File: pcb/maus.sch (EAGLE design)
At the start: 82 parts, among them IC1 AD712R, Q1 BC817, Q2 BC817, Q3 BSL307SP, T1 BC847, T2 BC847, U1 ESP32-S2-WROOM, U2 CH340C, U3 CP2102, U4 LP3965EMP-3.3, U5 LSM9DS1TR

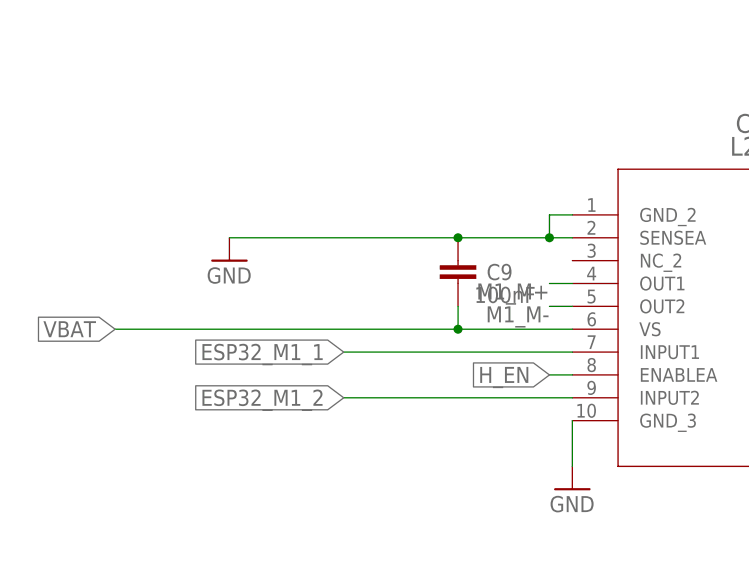
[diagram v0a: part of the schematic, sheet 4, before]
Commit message: Added 3.3V connection
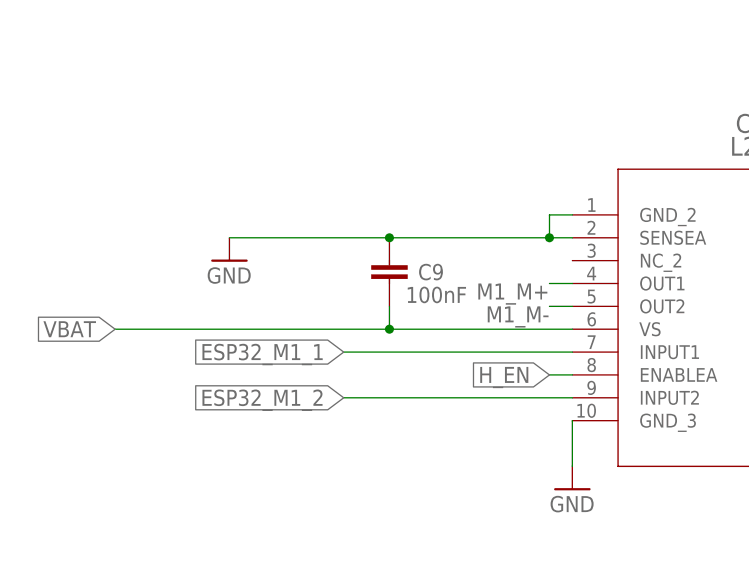
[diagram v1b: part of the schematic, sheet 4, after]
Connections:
- removed net N$2: C3.1, U2.V3
- net +3V3: now also C3.1, U2.V3
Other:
- moved on the sheet: C9
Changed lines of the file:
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@@
 <part name="GND40" library="supply1" library_urn="urn:adsk.eagle:library:371" deviceset="GND" device=""/>
 <part name="JP4" library="pinhead" library_urn="urn:adsk.eagle:library:325" deviceset="PINHD-1X6" device="" package3d_urn="urn:adsk.eagle:package:22472/2"/>
+<part name="+3V10" library="supply1" library_urn="urn:adsk.eagle:library:371" deviceset="+3V3" device=""/>
 </parts>
 <sheets>
@@
 <attribute name="VALUE" x="300.99" y="121.92" size="1.778" layer="96"/>
 </instance>
+<instance part="+3V10" gate="G$1" x="213.36" y="63.5" smashed="yes">
+<attribute name="VALUE" x="210.82" y="58.42" size="1.778" layer="96" rot="R90"/>
+</instance>
 </instances>
 <busses>
@@
 </segment>
 </net>
-<net name="N$2" class="0">
-<segment>
-<pinref part="U2" gate="G$1" pin="V3"/>
-<pinref part="C3" gate="G$1" pin="1"/>
-<wire x1="195.58" y1="55.88" x2="213.36" y2="55.88" width="0.1524" layer="91"/>
-</segment>
-</net>
 <net name="ESP32_TX" class="0">
 <segment>
@@
 <pinref part="+3V1" gate="G$1" pin="+3V3"/>
 <pinref part="JP4" gate="A" pin="5"/>
+</segment>
+<segment>
+<pinref part="U2" gate="G$1" pin="V3"/>
+<pinref part="C3" gate="G$1" pin="1"/>
+<wire x1="195.58" y1="55.88" x2="213.36" y2="55.88" width="0.1524" layer="91"/>
+<pinref part="+3V10" gate="G$1" pin="+3V3"/>
+<wire x1="213.36" y1="55.88" x2="213.36" y2="60.96" width="0.1524" layer="91"/>
+<junction x="213.36" y="55.88"/>
 </segment>
 </net>
@@
 </sheet>
 <sheet>
+<description>H-bridge motor driver</description>
 <plain>
 <text x="40.64" y="109.22" size="1.778" layer="91">Left Motor connector</text>
@@
 <attribute name="VALUE" x="123.444" y="15.621" size="1.778" layer="96"/>
 </instance>
-<instance part="C9" gate="G$1" x="60.96" y="35.56" smashed="yes" rot="R180">
-<attribute name="NAME" x="67.056" y="37.719" size="1.778" layer="95" rot="R180"/>
-<attribute name="VALUE" x="69.596" y="35.179" size="1.778" layer="96" rot="R180"/>
+<instance part="C9" gate="G$1" x="53.34" y="35.56" smashed="yes" rot="R180">
+<attribute name="NAME" x="59.436" y="37.719" size="1.778" layer="95" rot="R180"/>
+<attribute name="VALUE" x="61.976" y="35.179" size="1.778" layer="96" rot="R180"/>
 </instance>
 <instance part="GND31" gate="1" x="121.92" y="10.16" smashed="yes">
@@
 <pinref part="CR1" gate="A" pin="SENSEA"/>
 <wire x1="73.66" y1="40.64" x2="71.12" y2="40.64" width="0.1524" layer="91"/>
-<wire x1="71.12" y1="40.64" x2="60.96" y2="40.64" width="0.1524" layer="91"/>
+<wire x1="71.12" y1="40.64" x2="53.34" y2="40.64" width="0.1524" layer="91"/>
 <pinref part="CR1" gate="A" pin="GND_2"/>
 <wire x1="73.66" y1="43.18" x2="71.12" y2="43.18" width="0.1524" layer="91"/>
@@
 <junction x="71.12" y="40.64"/>
 <pinref part="C9" gate="G$1" pin="2"/>
-<junction x="60.96" y="40.64"/>
+<junction x="53.34" y="40.64"/>
 <pinref part="GND34" gate="1" pin="GND"/>
-<wire x1="60.96" y1="40.64" x2="35.56" y2="40.64" width="0.1524" layer="91"/>
+<wire x1="53.34" y1="40.64" x2="35.56" y2="40.64" width="0.1524" layer="91"/>
 </segment>
 <segment>
@@
 <segment>
 <pinref part="CR1" gate="A" pin="VS"/>
-<wire x1="73.66" y1="30.48" x2="60.96" y2="30.48" width="0.1524" layer="91"/>
-<wire x1="60.96" y1="30.48" x2="60.96" y2="33.02" width="0.1524" layer="91"/>
+<wire x1="73.66" y1="30.48" x2="53.34" y2="30.48" width="0.1524" layer="91"/>
+<wire x1="53.34" y1="30.48" x2="53.34" y2="33.02" width="0.1524" layer="91"/>
 <pinref part="C9" gate="G$1" pin="1"/>
-<junction x="60.96" y="30.48"/>
+<junction x="53.34" y="30.48"/>
 <label x="22.86" y="30.48" size="1.778" layer="95" rot="R180" xref="yes"/>
-<wire x1="60.96" y1="30.48" x2="22.86" y2="30.48" width="0.1524" layer="91"/>
-</segment>
-</net>
+<wire x1="53.34" y1="30.48" x2="22.86" y2="30.48" width="0.1524" layer="91"/>
+</segment>
+</net>

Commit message: Changed capacitor
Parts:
- C8, C9: device rcl:C-EU025-024X044 -> rcl:C-EUC0805
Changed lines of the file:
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@@
 <part name="JP2" library="pinhead" library_urn="urn:adsk.eagle:library:325" deviceset="PINHD-1X3" device="" package3d_urn="urn:adsk.eagle:package:22458/2"/>
 <part name="JP3" library="pinhead" library_urn="urn:adsk.eagle:library:325" deviceset="PINHD-1X3" device="" package3d_urn="urn:adsk.eagle:package:22458/2"/>
-<part name="C8" library="rcl" library_urn="urn:adsk.eagle:library:334" deviceset="C-EU" device="025-024X044" package3d_urn="urn:adsk.eagle:package:23630/1" value="100nF"/>
-<part name="C9" library="rcl" library_urn="urn:adsk.eagle:library:334" deviceset="C-EU" device="025-024X044" package3d_urn="urn:adsk.eagle:package:23630/1" value="100nF"/>
+<part name="C8" library="rcl" library_urn="urn:adsk.eagle:library:334" deviceset="C-EU" device="C0805" package3d_urn="urn:adsk.eagle:package:23617/2" value="100nF"/>
+<part name="C9" library="rcl" library_urn="urn:adsk.eagle:library:334" deviceset="C-EU" device="C0805" package3d_urn="urn:adsk.eagle:package:23617/2" value="100nF"/>
 <part name="IC1" library="analog-devices" library_urn="urn:adsk.eagle:library:102" deviceset="AD712" device="R" package3d_urn="urn:adsk.eagle:package:30987/2"/>
 <part name="P+2" library="supply1" library_urn="urn:adsk.eagle:library:371" deviceset="+5V" device=""/>

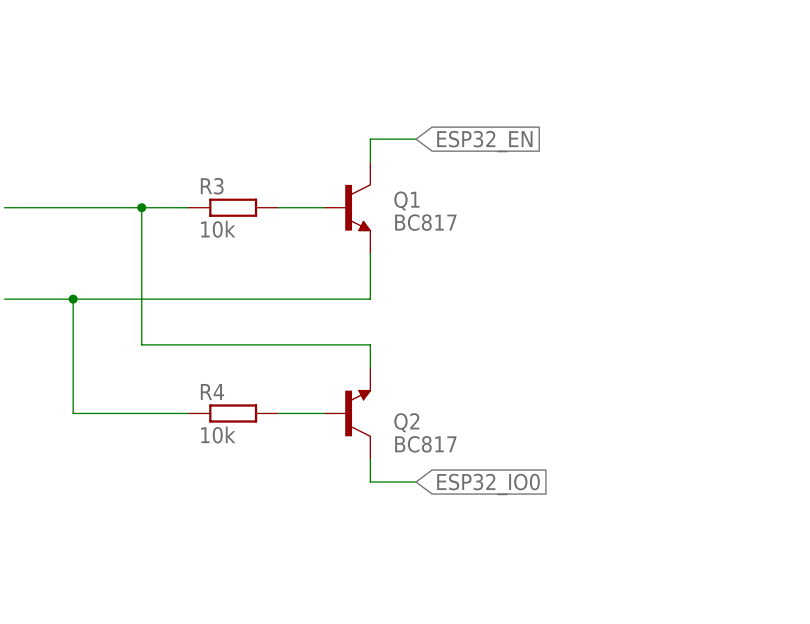
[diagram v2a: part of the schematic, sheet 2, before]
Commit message: Changed transistor type
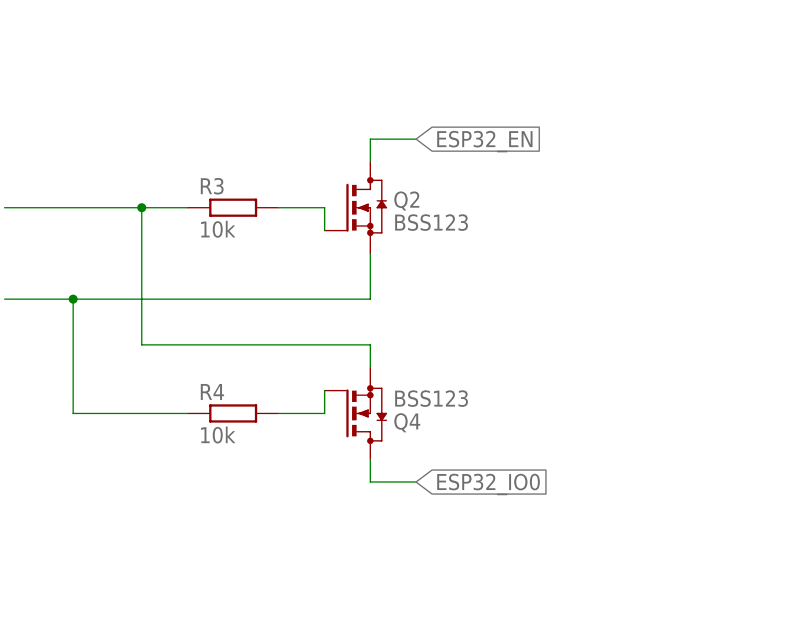
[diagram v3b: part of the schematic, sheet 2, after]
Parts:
- removed Q1: BC817, BC817:BC817
- added Q4: BSS123, transistor-small-signal:BSS123
- Q2: value BC817 -> BSS123; device BC817:BC817 -> transistor-small-signal:BSS123
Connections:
- net DTR: now also Q4.S; no longer Q2.E
- net ESP32_EN: now also Q2.D; no longer Q1.C
- net ESP32_IO0: now also Q4.D; no longer Q2.C
- net N$5: now also Q2.G; no longer Q1.B
- net N$6: now also Q4.G; no longer Q2.B
- net RTS: now also Q2.S; no longer Q1.E
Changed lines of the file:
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@@
 <part name="GND27" library="supply1" library_urn="urn:adsk.eagle:library:371" deviceset="GND" device=""/>
 <part name="R3" library="rcl" library_urn="urn:adsk.eagle:library:334" deviceset="R-EU_" device="R0805" package3d_urn="urn:adsk.eagle:package:23553/2" value="10k"/>
-<part name="Q1" library="BC817" deviceset="BC817" device=""/>
-<part name="Q2" library="BC817" deviceset="BC817" device=""/>
 <part name="R4" library="rcl" library_urn="urn:adsk.eagle:library:334" deviceset="R-EU_" device="R0805" package3d_urn="urn:adsk.eagle:package:23553/2" value="10k"/>
 <part name="D2" library="SparkFun-LED" library_urn="urn:adsk.eagle:library:529" deviceset="LED-RED" device="0603" package3d_urn="urn:adsk.eagle:package:39354/1" value="OK"/>
@@
 <part name="JP4" library="pinhead" library_urn="urn:adsk.eagle:library:325" deviceset="PINHD-1X6" device="" package3d_urn="urn:adsk.eagle:package:22472/2"/>
 <part name="+3V10" library="supply1" library_urn="urn:adsk.eagle:library:371" deviceset="+3V3" device=""/>
+<part name="Q4" library="transistor-small-signal" library_urn="urn:adsk.eagle:library:401" deviceset="BSS123" device="" package3d_urn="urn:adsk.eagle:package:28738/2"/>
+<part name="Q2" library="transistor-small-signal" library_urn="urn:adsk.eagle:library:401" deviceset="BSS123" device="" package3d_urn="urn:adsk.eagle:package:28738/2"/>
 </parts>
 <sheets>
@@
 <attribute name="VALUE" x="49.53" y="55.118" size="1.778" layer="96"/>
 </instance>
-<instance part="Q1" gate="G$1" x="66.04" y="58.42" smashed="yes">
-<attribute name="NAME" x="71.12" y="58.42" size="1.778" layer="95"/>
-<attribute name="VALUE" x="71.12" y="55.88" size="1.778" layer="96"/>
-</instance>
-<instance part="Q2" gate="G$1" x="66.04" y="35.56" smashed="yes" rot="MR180">
-<attribute name="NAME" x="71.12" y="35.56" size="1.778" layer="95" rot="MR180"/>
-<attribute name="VALUE" x="71.12" y="33.02" size="1.778" layer="96" rot="MR180"/>
-</instance>
 <instance part="R4" gate="G$1" x="53.34" y="35.56" smashed="yes">
 <attribute name="NAME" x="49.53" y="37.0586" size="1.778" layer="95"/>
@@
 <instance part="+3V10" gate="G$1" x="213.36" y="63.5" smashed="yes">
 <attribute name="VALUE" x="210.82" y="58.42" size="1.778" layer="96" rot="R90"/>
+</instance>
+<instance part="Q4" gate="G$1" x="68.58" y="35.56" smashed="yes" rot="MR180">
+<attribute name="NAME" x="71.12" y="35.56" size="1.778" layer="95" rot="MR180"/>
+<attribute name="VALUE" x="71.12" y="38.1" size="1.778" layer="96" rot="MR180"/>
+</instance>
+<instance part="Q2" gate="G$1" x="68.58" y="58.42" smashed="yes">
+<attribute name="NAME" x="71.12" y="58.42" size="1.778" layer="95"/>
+<attribute name="VALUE" x="71.12" y="55.88" size="1.778" layer="96"/>
 </instance>
 </instances>
@@
 <wire x1="43.18" y1="43.18" x2="68.58" y2="43.18" width="0.1524" layer="91"/>
 <junction x="43.18" y="58.42"/>
-<pinref part="Q2" gate="G$1" pin="E"/>
 <wire x1="68.58" y1="43.18" x2="68.58" y2="40.64" width="0.1524" layer="91"/>
+<pinref part="Q4" gate="G$1" pin="S"/>
 </segment>
 <segment>
@@
 <segment>
 <wire x1="27.94" y1="48.26" x2="35.56" y2="48.26" width="0.1524" layer="91"/>
-<pinref part="Q1" gate="G$1" pin="E"/>
 <wire x1="35.56" y1="48.26" x2="68.58" y2="48.26" width="0.1524" layer="91"/>
 <wire x1="68.58" y1="48.26" x2="68.58" y2="53.34" width="0.1524" layer="91"/>
@@
 <pinref part="R4" gate="G$1" pin="1"/>
 <wire x1="35.56" y1="35.56" x2="48.26" y2="35.56" width="0.1524" layer="91"/>
+<pinref part="Q2" gate="G$1" pin="S"/>
 </segment>
 <segment>
@@
 <pinref part="R3" gate="G$1" pin="2"/>
 <wire x1="58.42" y1="58.42" x2="63.5" y2="58.42" width="0.1524" layer="91"/>
-<pinref part="Q1" gate="G$1" pin="B"/>
+<pinref part="Q2" gate="G$1" pin="G"/>
+<wire x1="63.5" y1="58.42" x2="63.5" y2="55.88" width="0.1524" layer="91"/>
 </segment>
 </net>
 <net name="ESP32_EN" class="0">
 <segment>
-<pinref part="Q1" gate="G$1" pin="C"/>
 <wire x1="68.58" y1="63.5" x2="68.58" y2="66.04" width="0.1524" layer="91"/>
 <wire x1="68.58" y1="66.04" x2="73.66" y2="66.04" width="0.1524" layer="91"/>
 <label x="73.66" y="66.04" size="1.778" layer="95" xref="yes"/>
+<pinref part="Q2" gate="G$1" pin="D"/>
 </segment>
 </net>
@@
 <segment>
 <pinref part="R4" gate="G$1" pin="2"/>
-<pinref part="Q2" gate="G$1" pin="B"/>
 <wire x1="58.42" y1="35.56" x2="63.5" y2="35.56" width="0.1524" layer="91"/>
+<pinref part="Q4" gate="G$1" pin="G"/>
+<wire x1="63.5" y1="35.56" x2="63.5" y2="38.1" width="0.1524" layer="91"/>
 </segment>
 </net>
 <net name="ESP32_IO0" class="0">
 <segment>
-<pinref part="Q2" gate="G$1" pin="C"/>
 <wire x1="68.58" y1="30.48" x2="68.58" y2="27.94" width="0.1524" layer="91"/>
 <wire x1="68.58" y1="27.94" x2="73.66" y2="27.94" width="0.1524" layer="91"/>
 <label x="73.66" y="27.94" size="1.778" layer="95" xref="yes"/>
-</segment>
-</net>
+<pinref part="Q4" gate="G$1" pin="D"/>
+</segment>
+</net>
